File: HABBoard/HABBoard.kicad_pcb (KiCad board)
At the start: 4 copper layers, 100 x 100 mm, 212 parts, among them J1 USB_C_MCU, J10 RFShield_TwoPieces, J2 USB_C_GNSS, J3 MEM2067-02-180-00-A_REVB, J4 GPS In, J5 GNSS_UART, J6 DEBUG, J7 VHF Out, J8 UHF Out, J9 RFShield_TwoPieces, Q1 SSM6N7002KFU, Q2 SSM6N7002KFU, Q3 SSM6N7002KFU, Q4 PMN16XNE, SW1 RESET, SW2 BOOT, SW3 USER_BUTTON, SW4 Power, U1 TC2015-3.3VxCTTR, U10 SX1276, U11 SX1276, U12 MP5016GQH-Z, U13 PE42421, U14 ISL91127IR, U15 TPS2116DRLR, U16 INA219BxD, U2 W25Q128JVS, U3 NEO-M9N-00B, U4 AP2138N-2.5, U5 RP2040, U6 BME680, U7 TXS0104E, U8 ICM-20948, U9 AP2138N-1.8, Y1 ECS-TXO-25CSMV-320-BM-TR, Y2 ECS-TXO-25CSMV-320-BM-TR, Y3 12.000MHz

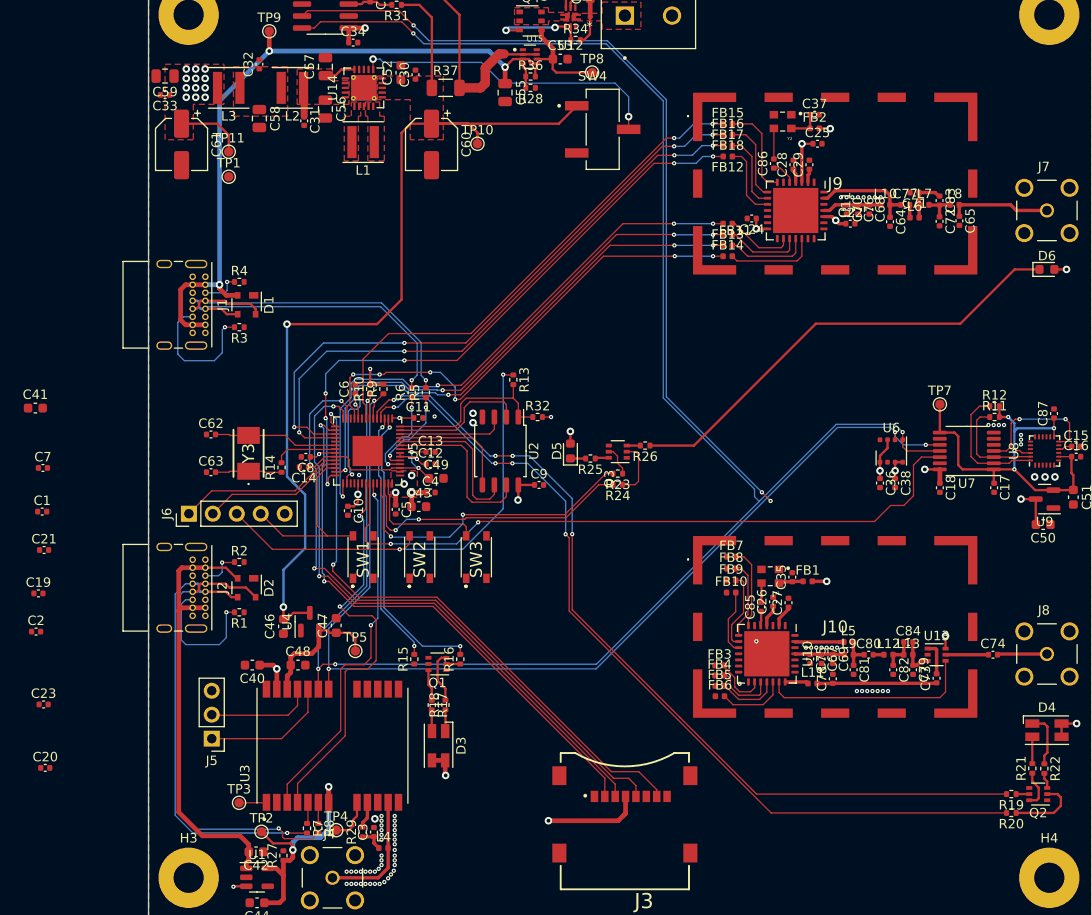
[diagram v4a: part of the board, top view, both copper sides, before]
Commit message: Finish majority of routing
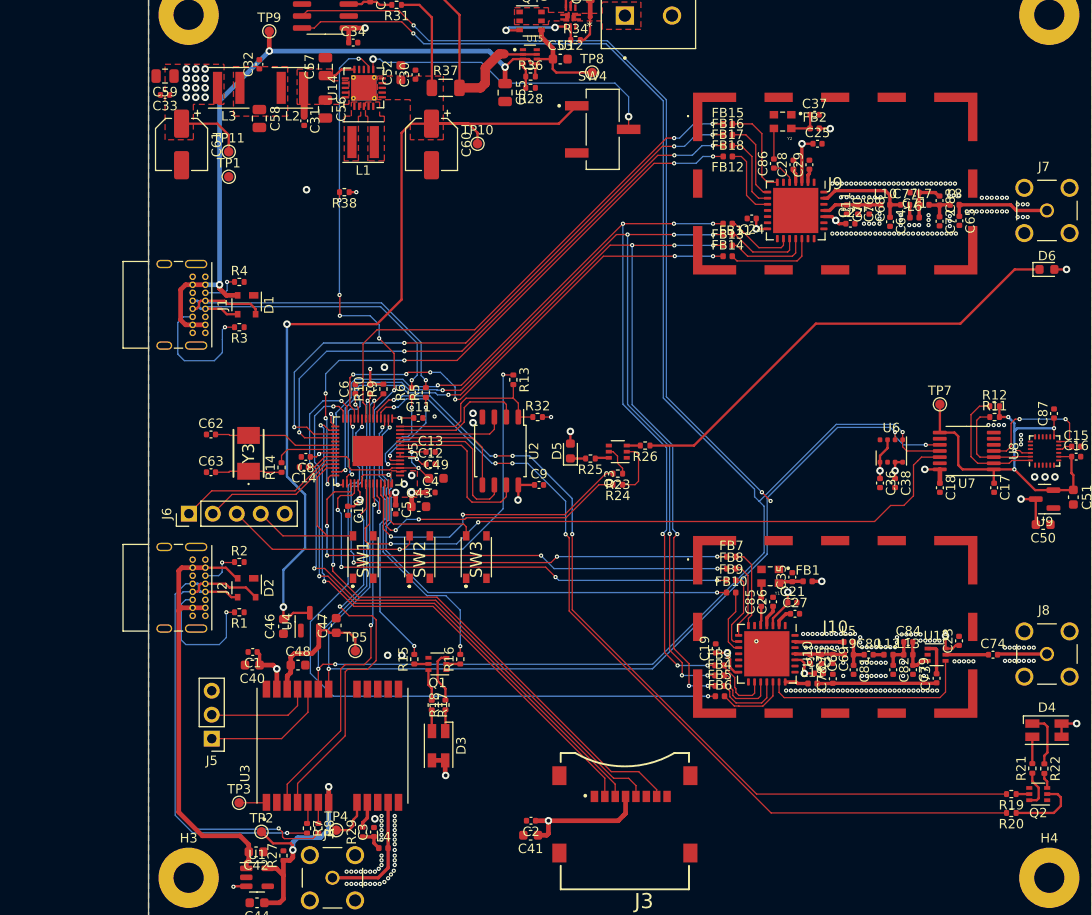
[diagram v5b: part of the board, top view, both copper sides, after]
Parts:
- removed C7: 0.1u, Capacitor_SMD:C_0402_1005Metric
- added R38: 10k, Resistor_SMD:R_0402_1005Metric, F.Cu at (48.5, 48.1)
- moved C23 97.3 mm to (113.7, 95.6), turned to 90 degrees
- moved C20 82.6 mm to (98.8, 99.1)
- moved C21 79.5 mm to (96.0, 91.6)
- moved C19 72.0 mm to (87.9, 96.4), turned to 90 degrees
- moved C41 69.3 mm to (68.3, 116.2), turned to 180 degrees
- moved C2 56.2 mm to (68.3, 114.7), turned to 180 degrees
- moved C1 26.8 mm to (38.8, 96.8), turned to 180 degrees
- moved C27 1.36 mm to (96.3, 92.8), turned to 0 degrees
- moved C85 0.54 mm to (92.7, 91.5)
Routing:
- net /UHF_NSS: track 0.00 -> 73.8 mm, vias 0 -> 2
- net /SMPS_MODE: track 0.00 -> 60.6 mm, vias 0 -> 7
- net /UHF_RESET: track 0.00 -> 56.6 mm, vias 0 -> 4
- net /RF_MISO: track 57.1 -> 109.7 mm, vias 4 -> 8
- net /UHF_DIO0: track 0.00 -> 52.6 mm, vias 0 -> 4
- net /RF_MOSI: track 57.7 -> 110.0 mm, vias 4 -> 8
- net /UHF_DIO1: track 0.00 -> 51.9 mm, vias 0 -> 4
- net /RF_SCK: track 61.1 -> 112.8 mm, vias 4 -> 8
- net /UHF_DIO2: track 0.00 -> 50.1 mm, vias 0 -> 2
- net +3V3: track 89.8 -> 108.7 mm, vias 42 -> 46
- net /BME_SCL: track 203.0 -> 206.9 mm
- net /BME_SDA: track 203.4 -> 206.9 mm
- net Net-(Q1-Pad5): track 0.00 -> 1.50 mm
- net Net-(FB5-Pad2): track 6.51 -> 7.50 mm
- net /VHF_RESET: track 54.9 -> 55.9 mm
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
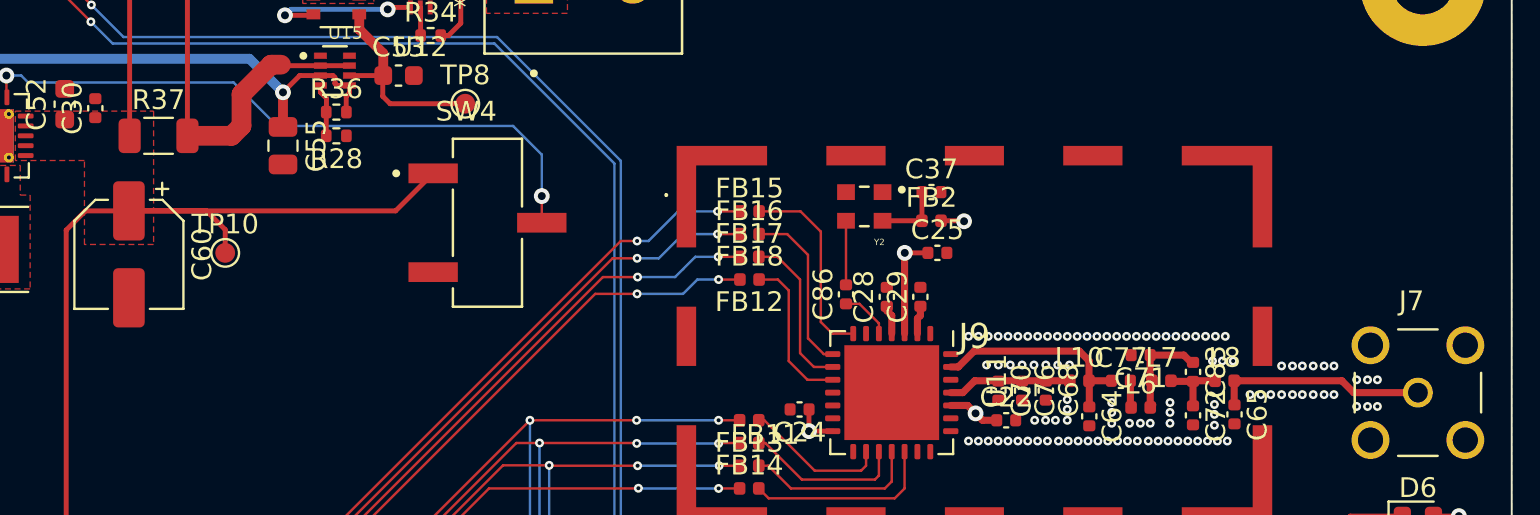
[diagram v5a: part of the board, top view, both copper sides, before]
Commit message: Fix PCB plane issues
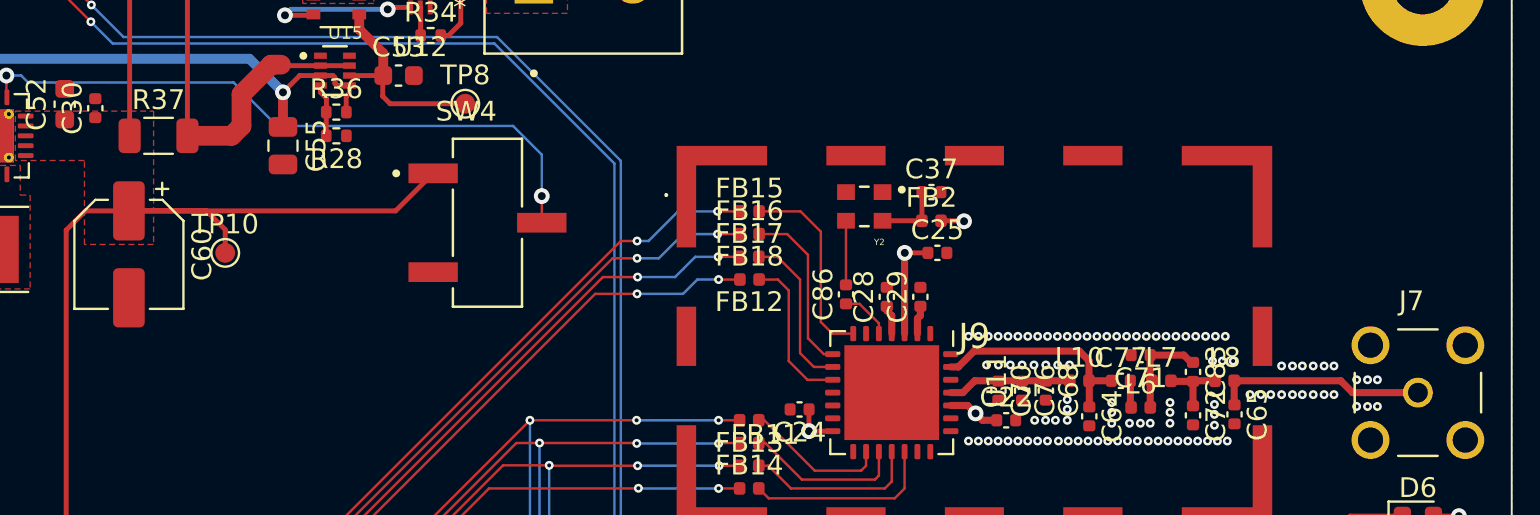
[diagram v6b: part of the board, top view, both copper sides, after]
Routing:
- added copper zone on In1.Cu, net GND
- removed copper zone on In2.Cu, net GND
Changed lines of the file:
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@@
     (fp_line (start -1.6 -0.8) (end 1.6 -0.8) (layer "F.Fab") (width 0.1))
     (fp_line (start -1.6 0.8) (end -1.6 -0.8) (layer "F.Fab") (width 0.1))
-    (pad "1" smd roundrect (at -1.4625 0) (size 1.125 1.75) (layers "F.Cu" "F.Paste" "F.Mask") (roundrect_rratio 0.222222)
+    (pad "1" smd roundrect (at -1.4625 0) (size 1.125 1.75) (layers "F.Cu" "F.Paste" "F.Mask") (roundrect_rratio 0.2222222222)
       (net 12 "+SYS") (pintype "passive"))
-    (pad "2" smd roundrect (at 1.4625 0) (size 1.125 1.75) (layers "F.Cu" "F.Paste" "F.Mask") (roundrect_rratio 0.222222)
+    (pad "2" smd roundrect (at 1.4625 0) (size 1.125 1.75) (layers "F.Cu" "F.Paste" "F.Mask") (roundrect_rratio 0.2222222222)
       (net 148 "Net-(R30-Pad2)") (pintype "passive"))
     (model "${KICAD6_3DMODEL_DIR}/Resistor_SMD.3dshapes/R_1206_3216Metric.wrl"
@@
   (segment (start 99.3525 48.7) (end 99.733467 48.7) (width 0.36) (layer "F.Cu") (net 26))
   (segment (start 106.365 49.415) (end 106.35 49.4) (width 0.36) (layer "F.Cu") (net 26))
-  (segment (start 123 50) (end 119.75 50) (width 0.36) (layer "F.Cu") (net 27))
+  (segment (start 119.6944 50) (end 119.0944 49.4) (width 0.36) (layer "F.Cu") (net 27))
   (segment (start 113.7 49.4) (end 113.7 50.605) (width 0.36) (layer "F.Cu") (net 27))
-  (segment (start 119.15 49.4) (end 113.7 49.4) (width 0.36) (layer "F.Cu") (net 27))
+  (segment (start 123 50) (end 119.6944 50) (width 0.36) (layer "F.Cu") (net 27))
   (segment (start 113.7 50.605) (end 113.715 50.62) (width 0.36) (layer "F.Cu") (net 27))
   (segment (start 113.95 49.415) (end 113.935 49.4) (width 0.36) (layer "F.Cu") (net 27))
-  (segment (start 119.75 50) (end 119.15 49.4) (width 0.36) (layer "F.Cu") (net 27))
+  (segment (start 119.0944 49.4) (end 113.7 49.4) (width 0.36) (layer "F.Cu") (net 27))
   (segment (start 72 28.499873) (end 71.999874 28.499999) (width 0.25) (layer "F.Cu") (net 28))
   (segment (start 71.945 26.98) (end 72 27.035) (width 0.25) (layer "F.Cu") (net 28))
@@
     )
   )
-  (zone (net 2) (net_name "GND") (layers "F.Cu" "In2.Cu" "B.Cu") (name "Ground Plane") (hatch edge 0.508)
+  (zone (net 2) (net_name "GND") (layers "F.Cu" "In1.Cu" "B.Cu") (name "Ground Plane") (hatch edge 0.508)
     (connect_pads yes (clearance 0.2))
     (min_thickness 0.2) (filled_areas_thickness no)
